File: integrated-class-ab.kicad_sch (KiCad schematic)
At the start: 28 parts, among them J1001 TX_OUT_GAIN, U1001 SL9062D, U1002 LT1794

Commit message: more work
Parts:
- removed R1012: 50k, BR_Passives:RES-ADJ-SMD_3P-L3.8-W3.7_VGF39NCHXT, symbol BR_Passives_misc:POT_50k_VGF39NCHXT-B503
- removed TP1001: POT2, BR_Connectors:TEST-TH_BD2.54-P1.4_RED, symbol BR_Connectors:TP_Ring_PTH
- removed TP1002: POT1, BR_Connectors:TEST-TH_BD2.54-P1.4_RED, symbol BR_Connectors:TP_Ring_PTH
- added D1001: LBAV99W, BR_SOT:SOT-323, symbol BR_Diodes:D_LBAV99W
- added Q1001: MMBT3904W, Package_TO_SOT_SMD:SOT-323_SC-70, symbol BR_Transistors:BJT_N_MMBT3904W
- added R1012, R1016: 4k7, BR_Passives:C_0402_1005Metric-minimized, symbol BR_Resistors_0402:R_0402_4k7
- added R1017: 0R, BR_Passives:R_0402_1005Metric, symbol BR_Resistors_0402:R_0402_0R
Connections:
- net GND: now also D1001.2, R1016.2; no longer U1002.6 (SHDNREF)
- net TX_EN: now also R1012.1
- net VTX: now also R1017.1
- net at U1002.5 (SHDN): now also R1017.2
- new net: D1001.1, Q1001.1 (B), R1012.2
- new net: Q1001.2 (E), R1016.1
- new net: Q1001.3 (C), U1002.6 (SHDNREF)
- no-connect marks 0 -> 1
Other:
- note removed: "Measure resistance across test points to get actual R = 50k-{measured}"
- note removed: "SHDN pin also controls Class AB bias current. Ibias = 25.6*(TX_EN - 1.2V)/(R + 2k) When TX_EN High, pot gives range of 1mA-27mA"
- moved on the sheet: C1002, C1003, C1004, C1005, C1006, C1007, J1001, R1007, R1008, R1009, R1010, R1011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

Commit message: more work
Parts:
- C1001, C1002: symbol BR_Capacitors_0201:C_0201_100nF_25V_X7R_10% -> BR_Capacitors_0201:C_0201_100nF_25V_X5R_10%
- J1001: value TX_OUT_GAIN -> LABEL
- R1011: value 200R -> 2k; symbol BR_Resistors_0402:R_0402_200R -> BR_Resistors_0402:R_0402_2k; BRE Number BRE-000314 -> BRE-000324; JLCPCB Part Num C114764 -> C60488; Manufacturer Part Num RC0402FR-07200RL -> RC0402FR-072KL; Supplier Part Num 1 311-200LRCT-ND -> 311-2KLRCT-ND; Supplier Part Num 2 311-200LRTR-ND -> 311-2KLRTR-ND; Supplier Part Num 3 C114764 -> C60488
- R1013, R1014: value 1k -> 10k; footprint BR_Passives:C_1210_3225Metric-minimized -> BR_Passives:C_0402_1005Metric-minimized; symbol BR_Resistors_1210:R_1210_1k -> BR_Resistors_0402:R_0402_10k; BRE Number BRE-001256 -> BRE-000292; JLCPCB Part Num C2960861 -> C144807; Manufacturer FOJAN -> YAGEO; Manufacturer Part Num FRC1210F1001TS -> AC0402FR-0710KL; Supplier 1 (none) -> DigiKey; Supplier 2 (none) -> DigiKey; Supplier 3 (none) -> JLCPCB; Supplier Part Num 1 (none) -> YAG3436CT-ND; Supplier Part Num 2 (none) -> YAG3436TR-ND; Supplier Part Num 3 (none) -> C144807
- TP1003: value SIG_IN+ -> TP_RING_TH
- TP1004: value SIG_IN- -> TP_RING_TH

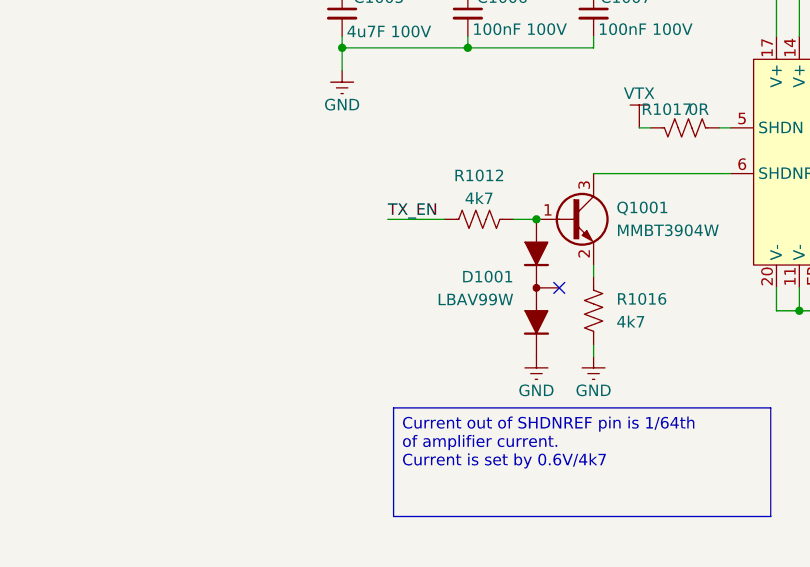
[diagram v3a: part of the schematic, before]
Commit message: refactoring interconnects to simplify busses
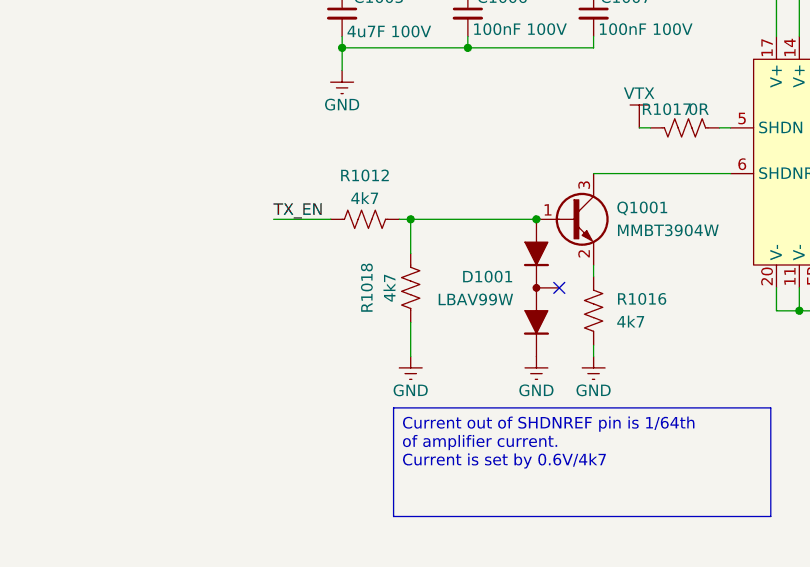
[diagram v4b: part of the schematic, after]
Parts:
- added R1018: 4k7, BR_Passives:C_0402_1005Metric-minimized, symbol BR_Resistors_0402:R_0402_4k7
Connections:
- net GND: now also R1018.1
- net at D1001.1, Q1001.1 (B), R1012.2: now also R1018.2
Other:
- moved on the sheet: R1012

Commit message: more work
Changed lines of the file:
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@@
 			)
 		)
-		(property "Datasheet" "https://jlc-prod-smt.oss-eu-central-1.aliyuncs.com/smtDataManualFile/8586176217171443712-C78879.pdf?response-content-disposition=attachment%3B%20filename%3DC78879.pdf%3B%20filename%2A%3DUTF-8%27%27C78879.pdf&x-oss-date=20260817T223541Z&x-oss-expires=1800&x-oss-security-token=CAISgAN1q6Ft5B2yfSjIr5vWEe7Wiap3hIqedUXns2kHOc5biqDfjzz2IHhMdHJsAOodtv0%2FmmhT6PkclqRLcbhpcmfjV%2BZHzLB8qZxKgHAo557b16cNrbH4M4H6aXeirtuwDsz9SNTCALjPD3nPii50x5bjaDymRCbLGJaViJlhHLN1Ow6jdmhpCctxLAlvo9NgFxm3D%2Fu2NQPwiWf9FVdhvhEG6Vly8qOi2MaRmFy8yFTx0b0SvJ%2BjYMrmPctoN9JnSdC5mfdzau3a1TJ84gRD0a5wkaVA1zbDs5bfISEIuUzebreLqY03dV4mOvdqIcMe8qigz88fk%2FfIioH6xyxKOexoSCnFTOiiupCcQLPyao9jLu6iayqViY7QaIOTqQohZmkAMwVOasAsI3Ngh4zF97Qt0cVNkXO9gWfLI8DtuMleWgpjVU%2FfNjvyAFpORa%2Bb5wchMHn6pr9EWOXuJZUIn3b%2FstWNupKq5ldctHSeoXq108CXVnU5PXYIECCz96KWD5sagAFwtYBqFGKfRHVxByVFm9hR5%2BknzEms19%2BxVKMA%2BH%2Fe0DXpHkXC%2BhvU13y0gz%2BY23wCeTpxhCwVBrtH081zQyZ7soqNYgAtwXed59cOXGPPo3MbUpdsEwRRehlgawQAABu3UJ4Q4Csv%2BVnTVIsBEUpJm%2BmrBBx8NwWeOtQ6JedWfSAA&x-oss-signature-version=OSS4-HMAC-SHA256&x-oss-credential=STS.NXcZTbduV3HuwcVWiR5Aweetm%2F20260817%2Feu-central-1%2Foss%2Faliyun_v4_request&x-oss-signature=50931d301ee03bfc0fdf0ba4de036e20837b4daa91ed3b92a5f7eba552f257a2"
+		(property "Datasheet" "https://jlc-prod-smt.oss-eu-central-1.aliyuncs.com/smtDataManualFile/8586176217171443712-C78879.pdf?response-content-disposition=attachment%3B%20filename%3DC78879.pdf%3B%20filename%2A%3DUTF-8%27%27C78879.pdf&x-oss-date=20260827T165022Z&x-oss-expires=1800&x-oss-security-token=CAISgAN1q6Ft5B2yfSjIr5rBf46Dm%2BkUjoffTmfrj0RmZt0VlZbIgDz2IHhMdHJsAOodtv0%2FmmhT6PkclqRLcbhpcmfjV%2BZHzLB8qd9020Et557b16cNrbH4M4H6aXeirtuwDsz9SNTCALjPD3nPii50x5bjaDymRCbLGJaViJlhHLN1Ow6jdmhpCctxLAlvo9NgFxm3D%2Fu2NQPwiWf9FVdhvhEG6Vly8qOi2MaRmFy8yFTx0b0SvJ%2BjYMrmPctoN9JnSdC5mfdzau3a1TJ84gRD0a5wkaVA1zbDs5bfISEIuUzebreLqY03dV4mOvdqIcMe8qigz88fk%2FfIioH6xyxKOexoSCnFTOiiupCcQLPyao9jLu6iayqViY7QaIOTqQohZmkAMwVOasAsI3Ngh4zF97Qt0cVNkXO9gWfLI8DtuMleWirPm07BHjvyAFpORa%2Bb5wchMHn6pr9EWOXuJZUIn3b%2FstWNupKq5ldctHSeoXq108CXVnU5PXYIAZogK6KWD5sagAEnYLRsdocKCbShdrg6Em3EA2acJQBrbyyBHCOtElBp9beg8NNhTqR5xZeFT8DMqT6kWMnQve6qTx3ZGWBk%2FxPyBnI4814DWDTC4OWLRLnxv%2F0HQewLCqXu%2Fgs87wJ76yDIDikMlXcfffQ%2Fqpq085YVdFxjTRx9EW5S%2B6H7Qi26qCAA&x-oss-signature-version=OSS4-HMAC-SHA256&x-oss-credential=STS.NYt447v659E4LAZkD3jR9zScb%2F20260827%2Feu-central-1%2Foss%2Faliyun_v4_request&x-oss-signature=819cafc7547a4bc2e84de4abe3f6c35e576a231bb5740d9233d4ec3d5ae0d456"
 			(at 313.69 201.93 0)
 			(hide yes)

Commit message: more work
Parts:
- renumbered C1005 to C1003, C1006 to C1004, C1007 to C1005, C1003 to C1006, C1004 to C1007, R1012 to R1007, R1018 to R1008, R1016 to R1009, R1017 to R1010, R1007 to R1011, R1008 to R1012, R1009 to R1013, R1010 to R1014, R1011 to R1015, R1013 to R1016, R1014 to R1017, TP1003 to TP1001, TP1004 to TP1002

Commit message: more work
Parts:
- R1011, R1012, R1013, R1014: value 100k -> 1M; footprint BR_Passives:R_0201_0603Metric-minimized -> BR_Passives:C_0402_1005Metric-minimized; symbol BR_Resistors_0201:R_0201_100k -> BR_Resistors_0402:R_0402_1M; BRE Number BRE-001166 -> BRE-000309; JLCPCB Part Num C106224 -> C144787; Manufacturer Part Num RC0201FR-07100KL -> AC0402FR-071ML; Supplier Part Num 1 311-10.0KMCT-ND -> YAG3450CT-ND; Supplier Part Num 2 603-RC0201FR-0710KL -> 603-AC0402FR-071ML; Supplier Part Num 3 C106225 -> C144787
- TP1001, TP1002: value TP_RING_TH -> value; footprint BR_Connectors:TEST-TH_BD2.54-P1.4_RED -> BR_Virtual_Parts:TP_PROBE_TIP_WITH_GND; symbol BR_Connectors:TP_Ring_PTH -> BR_Virtual_Parts:TP_Probe_Tip_0.8mm_Hole_with_GND; now left out of the parts list
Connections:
- net GND: now also TP1001.1, TP1002.1
- net SIG_IN+: now also TP1001.2 (GND); no longer TP1001.1
- net SIG_IN-: now also TP1002.2 (GND); no longer TP1002.1
- net TX_EN: no longer R1007.1
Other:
- moved on the sheet: C1003, C1004, C1005, C1006, C1007, D1001, J1001, Q1001, R1007, R1008, R1009, R1010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

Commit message: more work
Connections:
- net GND: now also TP1001.2 (GND), TP1002.2 (GND); no longer TP1001.1, TP1002.1
- net SIG_IN+: now also TP1001.1; no longer TP1001.2 (GND)
- net SIG_IN-: now also TP1002.1; no longer TP1002.2 (GND)
- net TX_EN: now also R1007.1
- net VTX renamed VRAIL
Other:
- moved on the sheet: TP1001, TP1002
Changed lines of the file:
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@@
 	)
 	(label "TX_EN"
-		(at 287.02 115.57 0)
+		(at 149.86 196.85 0)
 		(effects
 			(font
@@
 		)
 	)
-	(hierarchical_label "VTX"
+	(hierarchical_label "VRAIL"
 		(shape input)
 		(at 41.91 74.93 180)
@@
 			)
 		)
-		(property "Value" "VTX"
+		(property "Value" "VRAIL"
 			(at 157.48 166.37 0)
 			(show_name no)
@@
 			)
 		)
-		(property "Value" "VTX"
+		(property "Value" "VRAIL"
 			(at 181.61 95.25 0)
 			(show_name no)
@@
 			)
 		)
-		(property "Value" "VTX"
+		(property "Value" "VRAIL"
 			(at 190.5 182.88 0)
 			(show_name no)
@@
 		(property "Value" "1M"
 			(at 181.864 72.39 0)
+			(hide yes)
 			(show_name no)
 			(do_not_autoplace no)
@@
 			)
 		)
-		(property "Value" "VTX"
+		(property "Value" "VRAIL"
 			(at 49.53 71.12 0)
 			(show_name no)
@@
 	(symbol
 		(lib_id "BR_Virtual_Parts:TP_Probe_Tip_0.8mm_Hole_with_GND")
-		(at 149.86 88.9 270)
-		(mirror x)
+		(at 149.86 88.9 0)
 		(unit 1)
 		(body_style 1)
@@
 		(dnp no)
 		(property "Reference" "TP1002"
-			(at 149.86 85.09 90)
+			(at 155.702 88.9 0)
 			(show_name no)
 			(do_not_autoplace no)
@@
 		)
 		(property "Value" "value"
-			(at 160.02 110.49 0)
+			(at 128.27 78.74 0)
 			(hide yes)
 			(show_name no)
@@
 		)
 		(property "Footprint" "BR_Virtual_Parts:TP_PROBE_TIP_WITH_GND"
-			(at 157.226 87.63 0)
+			(at 151.13 81.534 0)
 			(hide yes)
 			(show_name no)
@@
 		)
 		(property "Datasheet" "https://wmsc.lcsc.com/wmsc/upload/file/pdf/v2/lcsc/2307040929_ronghe-RH-5000_C5277086.pdf"
-			(at 157.353 88.646 0)
+			(at 150.114 81.407 0)
 			(hide yes)
 			(show_name no)
@@
 		)
 		(property "Description" "Probe tip test pad"
-			(at 154.94 102.87 0)
+			(at 135.89 83.82 0)
 			(hide yes)
 			(show_name no)
@@
 		)
 		(property "Manufacturer" "ronghe"
-			(at 218.44 88.9 0)
+			(at 149.86 20.32 0)
 			(hide yes)
 			(show_name no)
@@
 		)
 		(property "Manufacturer Part Num" "RH-5000"
-			(at 215.9 88.9 0)
+			(at 149.86 22.86 0)
 			(hide yes)
 			(show_name no)
@@
 		)
 		(property "BRE Number" "BRE-000074"
-			(at 213.36 88.9 0)
+			(at 149.86 25.4 0)
 			(hide yes)
 			(show_name no)
@@
 		)
 		(property "Supplier 1" "DigiKey"
-			(at 210.82 88.9 0)
+			(at 149.86 27.94 0)
 			(hide yes)
 			(show_name no)
@@
 		)
 		(property "Supplier Part Num 1" ""
-			(at 208.28 88.9 0)
+			(at 149.86 30.48 0)
 			(hide yes)
 			(show_name no)
@@
 		)
 		(property "Supplier 2" "Mouser"
-			(at 205.74 88.9 0)
+			(at 149.86 33.02 0)
 			(hide yes)
 			(show_name no)
@@
 		)
 		(property "Supplier Part Num 2" ""
-			(at 203.2 88.9 0)
+			(at 149.86 35.56 0)
 			(hide yes)
 			(show_name no)
@@
 		)
 		(property "Supplier 3" "JLCPCB"
-			(at 200.66 88.9 0)
+			(at 149.86 38.1 0)
 			(hide yes)
 			(show_name no)
@@
 		)
 		(property "Supplier Part Num 3" "C5277086"
-			(at 198.12 88.9 0)
+			(at 149.86 40.64 0)
 			(hide yes)
 			(show_name no)
@@
 		)
 		(property "Label" "LABEL"
-			(at 195.58 88.9 0)
+			(at 149.86 43.18 0)
 			(hide yes)
 			(show_name no)
@@
 		)
 		(property "JLCPCB Part Num" "C5277086"
-			(at 193.04 88.9 0)
+			(at 149.86 45.72 0)
 			(hide yes)
 			(show_name no)
@@
 	(symbol
 		(lib_id "BR_Virtual_Parts:TP_Probe_Tip_0.8mm_Hole_with_GND")
-		(at 106.68 87.63 270)
-		(mirror x)
+		(at 106.68 87.63 0)
 		(unit 1)
 		(body_style 1)
@@
 		(dnp no)
 		(property "Reference" "TP1001"
-			(at 106.68 83.82 90)
+			(at 112.522 87.884 0)
 			(show_name no)
 			(do_not_autoplace no)
@@
 		)
 		(property "Value" "value"
-			(at 116.84 109.22 0)
+			(at 85.09 77.47 0)
 			(hide yes)
 			(show_name no)
@@
 		)
 		(property "Footprint" "BR_Virtual_Parts:TP_PROBE_TIP_WITH_GND"
-			(at 114.046 86.36 0)
+			(at 107.95 80.264 0)
 			(hide yes)
 			(show_name no)
@@
 		)
 		(property "Datasheet" "https://wmsc.lcsc.com/wmsc/upload/file/pdf/v2/lcsc/2307040929_ronghe-RH-5000_C5277086.pdf"
-			(at 114.173 87.376 0)
+			(at 106.934 80.137 0)
 			(hide yes)
 			(show_name no)
@@
 		)
 		(property "Description" "Probe tip test pad"
-			(at 111.76 101.6 0)
+			(at 92.71 82.55 0)
 			(hide yes)
 			(show_name no)
@@
 		)
 		(property "Manufacturer" "ronghe"
-			(at 175.26 87.63 0)
+			(at 106.68 19.05 0)
 			(hide yes)
 			(show_name no)
@@
 		)
 		(property "Manufacturer Part Num" "RH-5000"
-			(at 172.72 87.63 0)
+			(at 106.68 21.59 0)
 			(hide yes)
 			(show_name no)
@@
 		)
 		(property "BRE Number" "BRE-000074"
-			(at 170.18 87.63 0)
+			(at 106.68 24.13 0)
 			(hide yes)
 			(show_name no)
@@
 		)
 		(property "Supplier 1" "DigiKey"
-			(at 167.64 87.63 0)
+			(at 106.68 26.67 0)
 			(hide yes)
 			(show_name no)
@@
 		)
 		(property "Supplier Part Num 1" ""
-			(at 165.1 87.63 0)
+			(at 106.68 29.21 0)
 			(hide yes)
 			(show_name no)
@@
 		)
 		(property "Supplier 2" "Mouser"
-			(at 162.56 87.63 0)
+			(at 106.68 31.75 0)
 			(hide yes)
 			(show_name no)
@@
 		)
 		(property "Supplier Part Num 2" ""
-			(at 160.02 87.63 0)
+			(at 106.68 34.29 0)
 			(hide yes)
 			(show_name no)
@@
 		)
 		(property "Supplier 3" "JLCPCB"
-			(at 157.48 87.63 0)
+			(at 106.68 36.83 0)
 			(hide yes)
 			(show_name no)
@@
 		)
 		(property "Supplier Part Num 3" "C5277086"
-			(at 154.94 87.63 0)
+			(at 106.68 39.37 0)
 			(hide yes)
 			(show_name no)
@@
 		)
 		(property "Label" "LABEL"
-			(at 152.4 87.63 0)
+			(at 106.68 41.91 0)
 			(hide yes)
 			(show_name no)
@@
 		)
 		(property "JLCPCB Part Num" "C5277086"
-			(at 149.86 87.63 0)
+			(at 106.68 44.45 0)
 			(hide yes)
 			(show_name no)
@@
 			)
 		)
-		(property "Value" "VTX"
+		(property "Value" "VRAIL"
 			(at 180.34 49.784 0)
 			(show_name no)
